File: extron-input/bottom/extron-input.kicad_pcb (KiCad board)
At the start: 2 copper layers, 114 x 37 mm, 22 parts, among them J1 SCART-F, J10 Conn_01x01, J11 RED_N, J12 BLUE, J13 SYNC, J2 RED, J3 GREEN, J4 BLUE, J5 SYNC, J6 PHOENIX, J7 SENSE, J8 Conn_01x01, J9 Conn_01x01, SW1 SW_DPDT_x2, U1 LM1881

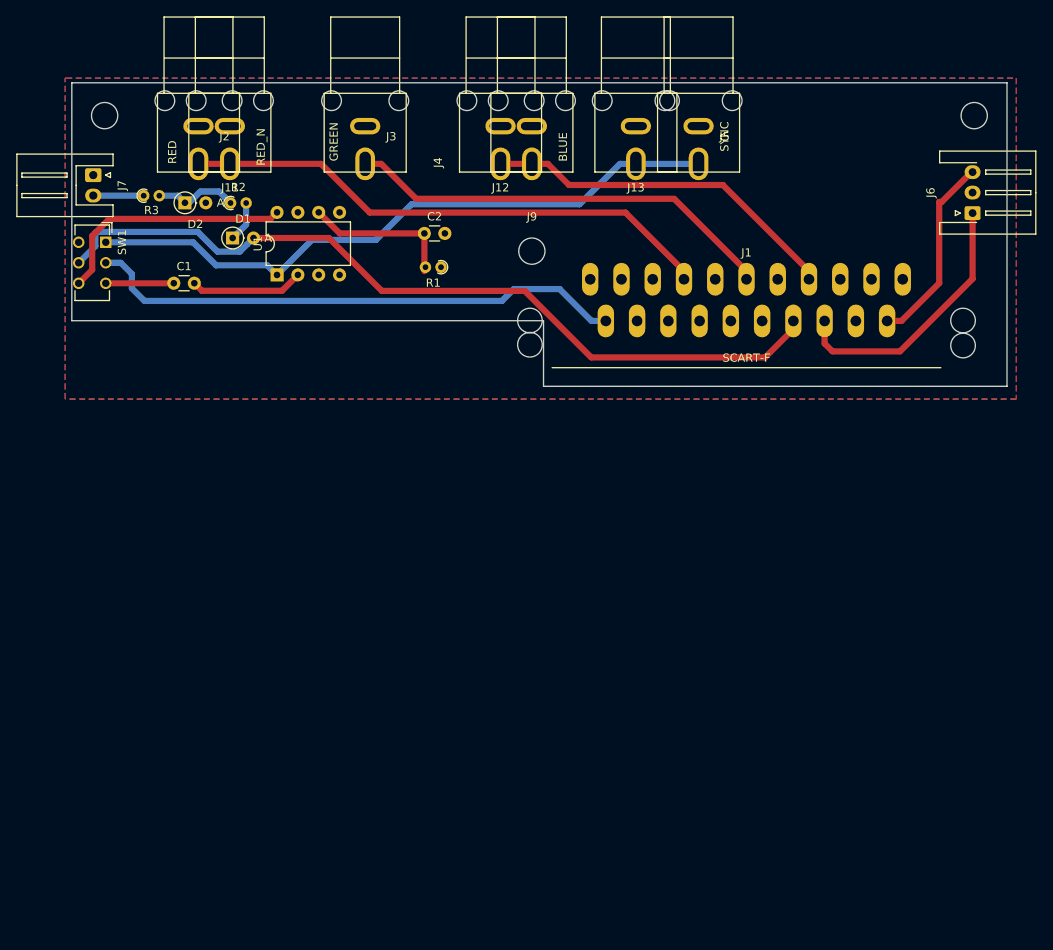
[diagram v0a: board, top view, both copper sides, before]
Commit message: Bottom board is now done(ish)
I've also aligned the mounting holes between the boards
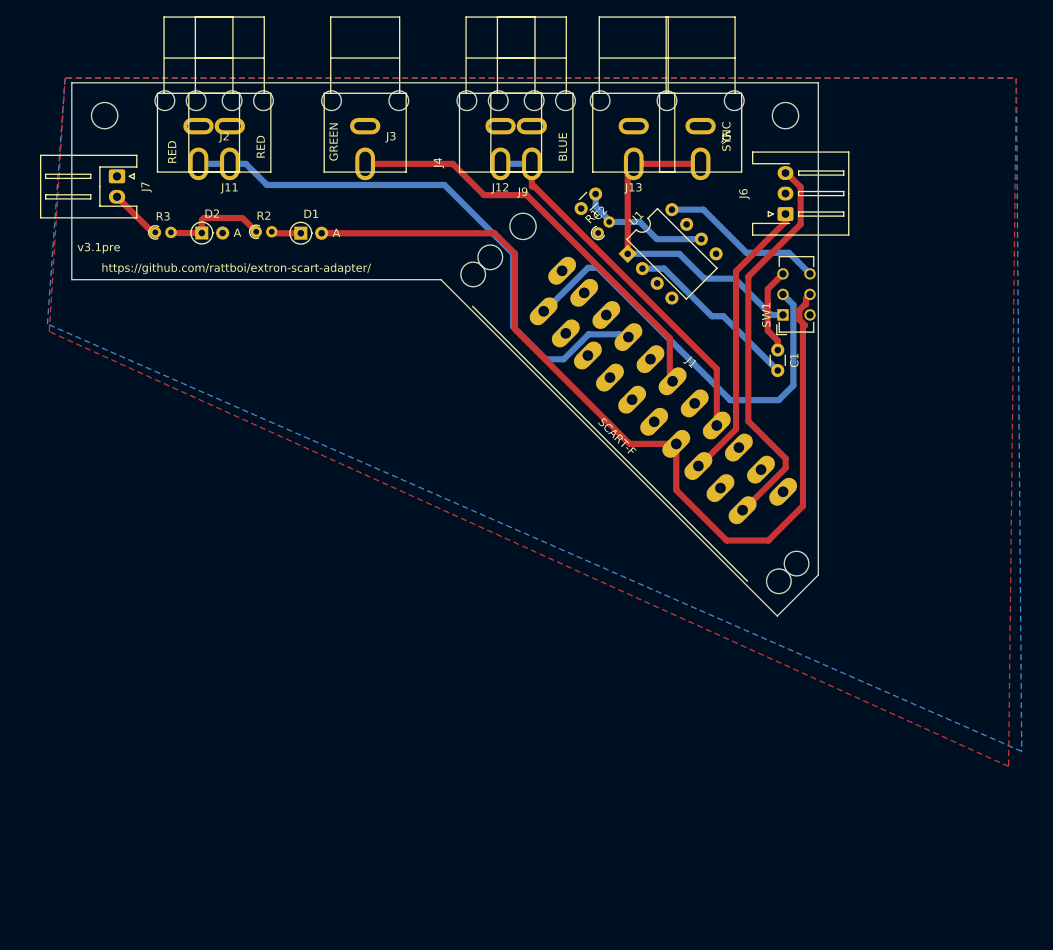
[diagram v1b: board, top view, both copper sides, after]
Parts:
- J11: value RED_N -> RED
- moved SW1 83.0 mm to (162.7, 104.3), turned to 90 degrees
- moved C1 74.1 mm to (162.1, 108.6), turned to 270 degrees
- moved U1 42.8 mm to (143.8, 96.9), turned to 45 degrees
- moved J8 23.0 mm to (163.0, 80.0)
- moved J6 22.8 mm to (163.0, 92.0)
- moved C2 21.4 mm to (139.9, 89.6), turned to 225 degrees
- moved R1 19.6 mm to (140.2, 94.3), turned to 45 degrees
- moved J1 16.7 mm to (145.6, 116.0), turned to 135 degrees
- moved D1 8.33 mm to (103.9, 94.3)
- moved R2 4.70 mm to (98.5, 94.2)
- moved R3 4.69 mm to (86.2, 94.2)
- moved D2 4.22 mm to (91.8, 94.3)
- moved J9 3.21 mm to (131.0, 93.5)
- moved J7 2.90 mm to (81.5, 87.4)
- moved J13 0.26 mm to (144.5, 81.3)
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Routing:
- net SYNC: track 79.5 -> 43.3 mm
- net Net-(J1-Pad2): track 23.7 -> 48.7 mm
- net Net-(J1-Pad20): track 66.1 -> 52.2 mm
- net SENSE: track 99.8 -> 111.6 mm
- net Net-(SW1-Pad6): track 30.2 -> 20.1 mm
- net Net-(C1-Pad2): track 13.8 -> 21.6 mm
- net BLUE: track 44.0 -> 48.4 mm
- net RED: track 65.6 -> 69.0 mm
- net Net-(J1-Pad6): track 32.9 -> 35.8 mm
- net Net-(D2-Pad1): track 10.2 -> 12.8 mm
- net Net-(C2-Pad1): track 18.5 -> 16.2 mm
- net Net-(C1-Pad1): track 8.30 -> 10.6 mm
- net Net-(D1-Pad1): track 4.95 -> 3.61 mm
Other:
- board size 114 x 37 mm -> 91 x 65 mm
- board text added: "v3.1pre"
- board text removed: "v3.0pre"

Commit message: Found a size for the bottom board that won't impede on the top board
These prototypes are sent off to JLC, so I'm also capturing the gerbers
in the repo.

V3.1pre

I think these have a good chance to be good...
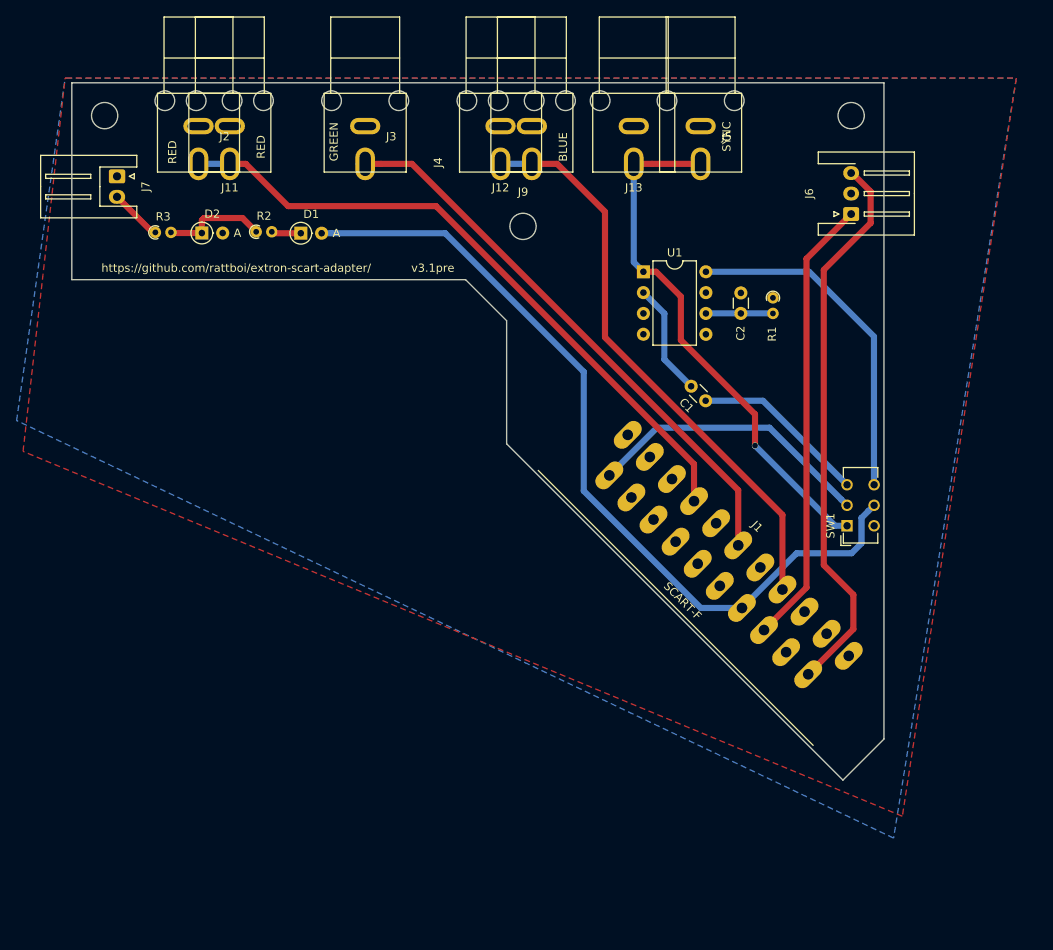
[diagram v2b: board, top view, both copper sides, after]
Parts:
- moved SW1 26.9 mm to (170.5, 130.0)
- moved C2 22.9 mm to (157.6, 104.1), turned to 90 degrees
- moved R1 22.7 mm to (161.5, 102.2), turned to 270 degrees
- moved J1 21.5 mm to (153.6, 136.0)
- moved C1 10.7 mm to (153.3, 114.8), turned to 135 degrees
- moved J6 8.00 mm to (171.0, 92.0)
- moved J8 8.00 mm to (171.0, 80.0)
- moved U1 2.90 mm to (145.7, 99.0), turned to 0 degrees
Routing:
- net SYNC: track 43.3 -> 66.7 mm, vias 0 -> 1
- net BLUE: track 48.4 -> 71.2 mm
- net Net-(SW1-Pad6): track 20.1 -> 41.8 mm
- net Net-(J1-Pad2): track 48.7 -> 68.3 mm
- net Net-(J1-Pad6): track 35.8 -> 55.1 mm
- net GREEN: track 52.5 -> 69.5 mm
- net Net-(J1-Pad20): track 52.2 -> 35.3 mm
- net RED: track 69.0 -> 80.4 mm
- net Net-(C1-Pad1): track 10.6 -> 21.5 mm
- net SENSE: track 111.6 -> 101.8 mm
- net Net-(C2-Pad1): track 16.2 -> 8.17 mm
- net Net-(C1-Pad2): track 21.6 -> 13.8 mm
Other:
- board size 91 x 65 mm -> 99 x 85 mm

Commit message: extron-input v3
Extended bottom board by 5mm
Fixed silkscreen up to be reasonable
Fixed up gitignore
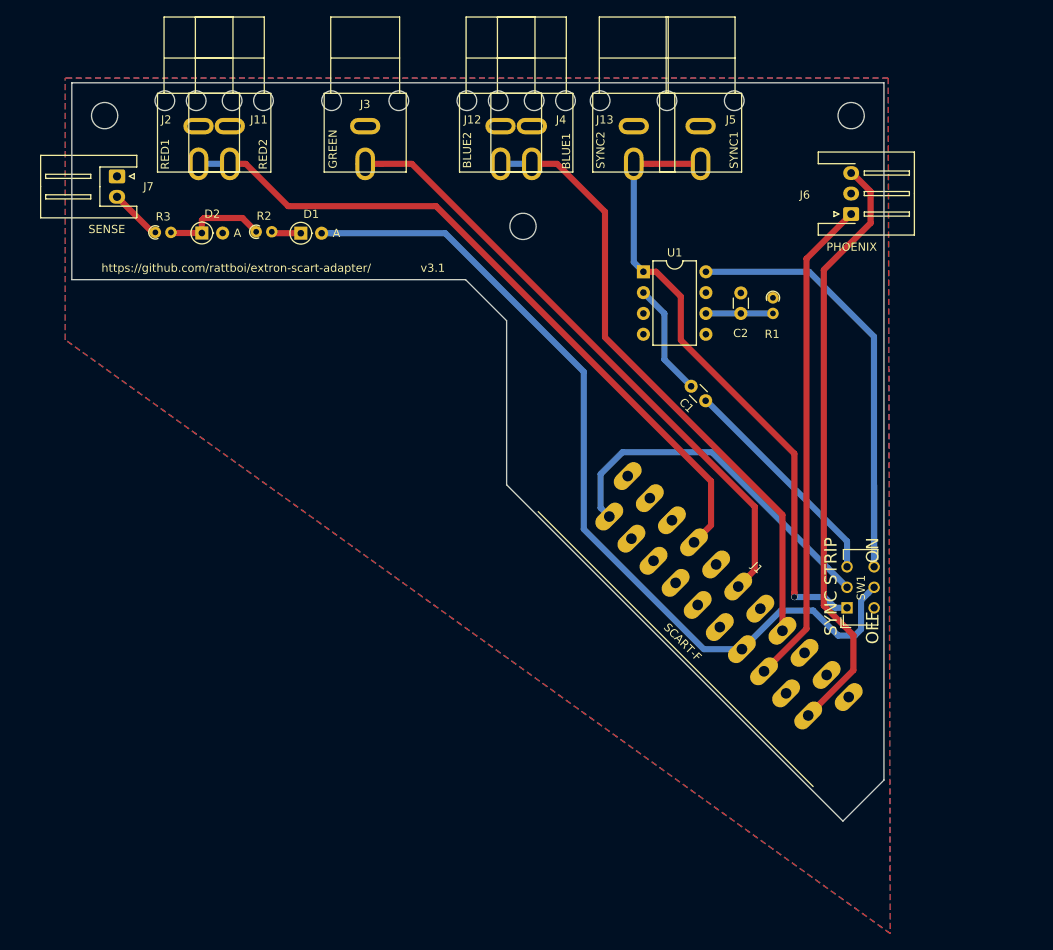
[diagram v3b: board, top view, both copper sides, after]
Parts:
- J11: value RED -> RED2
- J12: value BLUE -> BLUE2
- J13: value SYNC -> SYNC2
- J2: value RED -> RED1
- J4: value BLUE -> BLUE1
- J5: value SYNC -> SYNC1
- moved SW1 10.0 mm to (170.5, 140.0)
- moved J1 5.02 mm to (153.6, 141.0)
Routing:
- net Net-(SW1-Pad6): track 41.8 -> 61.8 mm
- net SYNC: track 66.7 -> 78.9 mm
- net Net-(J1-Pad20): track 35.3 -> 43.8 mm
- net RED: track 80.4 -> 87.1 mm
- net GREEN: track 69.5 -> 76.2 mm
- net Net-(C1-Pad1): track 21.5 -> 27.4 mm
- net SENSE: track 101.8 -> 107.3 mm
- net BLUE: track 71.2 -> 76.3 mm
- net Net-(J1-Pad6): track 55.1 -> 60.1 mm
- net Net-(J1-Pad2): track 68.3 -> 73.3 mm
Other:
- board size 99 x 85 mm -> 99 x 90 mm
- board text added: "OFF ON"
- board text added: "SYNC STRIP"
- board text added: "v3.1"
- board text removed: "v3.1pre"
